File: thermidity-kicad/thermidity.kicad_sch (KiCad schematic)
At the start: 13 parts, among them J1 ISP, J2 Display, U1 ATmega328P-P, U2 MCP1501-30xSN, U3 TMP36GT9, U4 HIH-5030-001

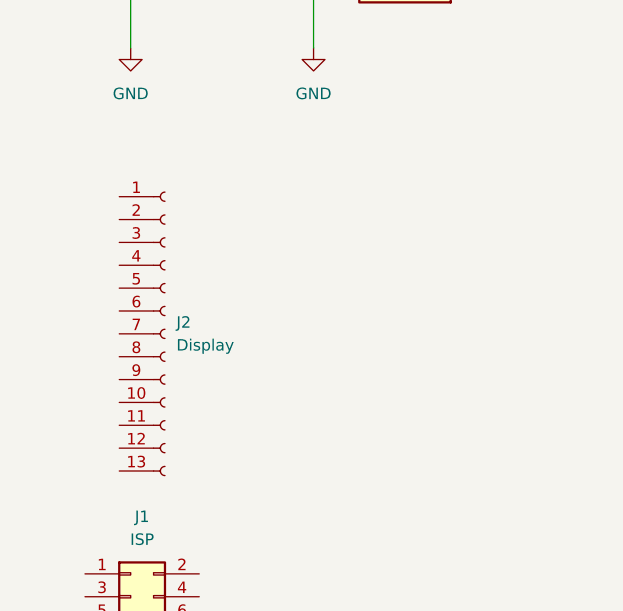
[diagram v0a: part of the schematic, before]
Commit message: update README, add crystal to schematic
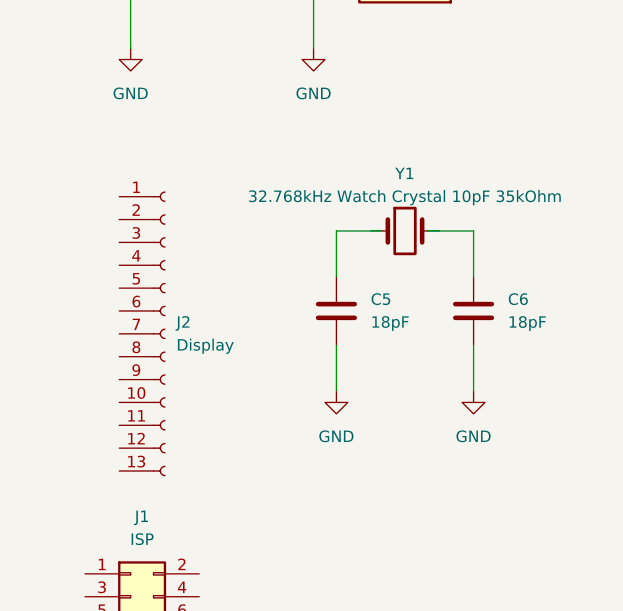
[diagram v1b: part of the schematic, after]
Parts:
- added C5, C6: 18pF, Capacitor_SMD:C_1206_3216Metric_Pad1.33x1.80mm_HandSolder, symbol Device:C
- added Y1: 32.768kHz Watch Crystal 10pF 35kOhm, symbol Device:Crystal
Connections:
- net GND: now also C5.2, C6.2
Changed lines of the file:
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@@
+    (stroke (width 0) (type default) (color 0 0 0 0))
+  )
+  (wire (pts (xy 214.63 113.03) (xy 214.63 118.11))
     (stroke (width 0) (type default) (color 0 0 0 0))
   )
@@
     (stroke (width 0) (type default) (color 0 0 0 0))
   )
+  (wire (pts (xy 214.63 100.33) (xy 214.63 105.41))
+    (stroke (width 0) (type default) (color 0 0 0 0))
+  )
+  (wire (pts (xy 209.55 100.33) (xy 214.63 100.33))
+    (stroke (width 0) (type default) (color 0 0 0 0))
+  )
   (wire (pts (xy 97.79 86.36) (xy 97.79 99.06))
     (stroke (width 0) (type default) (color 0 0 0 0))
@@
     (stroke (width 0) (type default) (color 0 0 0 0))
   )
+  (wire (pts (xy 199.39 100.33) (xy 199.39 105.41))
+    (stroke (width 0) (type default) (color 0 0 0 0))
+  )
   (wire (pts (xy 113.03 81.28) (xy 113.03 86.36))
     (stroke (width 0) (type default) (color 0 0 0 0))
@@
     (stroke (width 0) (type default) (color 0 0 0 0))
   )
+  (wire (pts (xy 199.39 113.03) (xy 199.39 118.11))
+    (stroke (width 0) (type default) (color 0 0 0 0))
+  )
   (wire (pts (xy 128.27 121.92) (xy 128.27 81.28))
     (stroke (width 0) (type default) (color 0 0 0 0))
@@
   )
   (wire (pts (xy 146.05 41.91) (xy 97.79 41.91))
+    (stroke (width 0) (type default) (color 0 0 0 0))
+  )
+  (wire (pts (xy 204.47 100.33) (xy 199.39 100.33))
     (stroke (width 0) (type default) (color 0 0 0 0))
   )
@@
     (pin "1")
   )
+  (symbol (lib_id "Device:C") (at 199.39 109.22 0) (unit 1)
+    (in_bom yes) (on_board yes) (fields_autoplaced)
+    (property "Reference" "C5" (id 0) (at 203.2 107.9499 0)
+      (effects (font (size 1.27 1.27)) (justify left))
+    )
+    (property "Value" "18pF" (id 1) (at 203.2 110.4899 0)
+      (effects (font (size 1.27 1.27)) (justify left))
+    )
+    (property "Footprint" "Capacitor_SMD:C_1206_3216Metric_Pad1.33x1.80mm_HandSolder" (id 2) (at 200.3552 113.03 0)
+      (effects (font (size 1.27 1.27)) hide)
+    )
+    (property "Datasheet" "~" (id 3) (at 199.39 109.22 0)
+      (effects (font (size 1.27 1.27)) hide)
+    )
+    (pin "1")
+    (pin "2")
+  )
   (symbol (lib_id "power:GND") (at 128.27 57.15 0) (unit 1)
     (in_bom yes) (on_board yes) (fields_autoplaced)
@@
     (pin "6")
   )
+  (symbol (lib_id "Device:Crystal") (at 207.01 100.33 0) (unit 1)
+    (in_bom yes) (on_board yes) (fields_autoplaced)
+    (property "Reference" "Y1" (id 0) (at 207.01 93.98 0))
+    (property "Value" "32.768kHz Watch Crystal 10pF 35kOhm" (id 1) (at 207.01 96.52 0))
+    (property "Footprint" "" (id 2) (at 207.01 100.33 0)
+      (effects (font (size 1.27 1.27)) hide)
+    )
+    (property "Datasheet" "~" (id 3) (at 207.01 100.33 0)
+      (effects (font (size 1.27 1.27)) hide)
+    )
+    (pin "1")
+    (pin "2")
+  )
   (symbol (lib_id "power:+BATT") (at 146.05 41.91 0) (unit 1)
     (in_bom yes) (on_board yes) (fields_autoplaced)
@@
     )
     (property "Datasheet" "" (id 3) (at 82.55 64.77 0)
+      (effects (font (size 1.27 1.27)) hide)
+    )
+    (pin "1")
+  )
+  (symbol (lib_id "power:GND") (at 199.39 118.11 0) (unit 1)
+    (in_bom yes) (on_board yes) (fields_autoplaced)
+    (property "Reference" "#PWR?" (id 0) (at 199.39 124.46 0)
+      (effects (font (size 1.27 1.27)) hide)
+    )
+    (property "Value" "GND" (id 1) (at 199.39 123.19 0))
+    (property "Footprint" "" (id 2) (at 199.39 118.11 0)
+      (effects (font (size 1.27 1.27)) hide)
+    )
+    (property "Datasheet" "" (id 3) (at 199.39 118.11 0)
       (effects (font (size 1.27 1.27)) hide)
     )
@@
     (pin "9")
   )
+  (symbol (lib_id "power:GND") (at 214.63 118.11 0) (unit 1)
+    (in_bom yes) (on_board yes) (fields_autoplaced)
+    (property "Reference" "#PWR?" (id 0) (at 214.63 124.46 0)
+      (effects (font (size 1.27 1.27)) hide)
+    )
+    (property "Value" "GND" (id 1) (at 214.63 123.19 0))
+    (property "Footprint" "" (id 2) (at 214.63 118.11 0)
+      (effects (font (size 1.27 1.27)) hide)
+    )
+    (property "Datasheet" "" (id 3) (at 214.63 118.11 0)
+      (effects (font (size 1.27 1.27)) hide)
+    )
+    (pin "1")
+  )
   (symbol (lib_id "Reference_Voltage:MCP1501-30xSN") (at 97.79 78.74 0) (unit 1)
     (in_bom yes) (on_board yes) (fields_autoplaced)
@@
     (pin "1")
   )
+  (symbol (lib_id "Device:C") (at 214.63 109.22 0) (unit 1)
+    (in_bom yes) (on_board yes) (fields_autoplaced)
+    (property "Reference" "C6" (id 0) (at 218.44 107.9499 0)
+      (effects (font (size 1.27 1.27)) (justify left))
+    )
+    (property "Value" "18pF" (id 1) (at 218.44 110.4899 0)
+      (effects (font (size 1.27 1.27)) (justify left))
+    )
+    (property "Footprint" "Capacitor_SMD:C_1206_3216Metric_Pad1.33x1.80mm_HandSolder" (id 2) (at 215.5952 113.03 0)
+      (effects (font (size 1.27 1.27)) hide)
+    )
+    (property "Datasheet" "~" (id 3) (at 214.63 109.22 0)
+      (effects (font (size 1.27 1.27)) hide)
+    )
+    (pin "1")
+    (pin "2")
+  )
   (symbol (lib_id "Device:R") (at 120.65 135.89 0) (unit 1)
     (in_bom yes) (on_board yes) (fields_autoplaced)
@@
       (reference "#PWR?") (unit 1) (value "GND") (footprint "")
     )
+    (path "/94bf8396-b53e-48d7-867c-3779df6a12e4"
+      (reference "#PWR?") (unit 1) (value "GND") (footprint "")
+    )
     (path "/a2d0e6a7-6199-4702-be53-1953075dda18"
+      (reference "#PWR?") (unit 1) (value "GND") (footprint "")
+    )
+    (path "/bf845653-5bee-4a32-b784-08641f731c62"
       (reference "#PWR?") (unit 1) (value "GND") (footprint "")
     )
@@
       (reference "C4") (unit 1) (value "100nF") (footprint "Capacitor_SMD:C_1206_3216Metric_Pad1.33x1.80mm_HandSolder")
     )
+    (path "/2782ed05-b38e-4160-a854-e129bce2a00e"
+      (reference "C5") (unit 1) (value "18pF") (footprint "Capacitor_SMD:C_1206_3216Metric_Pad1.33x1.80mm_HandSolder")
+    )
+    (path "/cd47be7e-fc20-4cc3-8eef-45df9b7c371f"
+      (reference "C6") (unit 1) (value "18pF") (footprint "Capacitor_SMD:C_1206_3216Metric_Pad1.33x1.80mm_HandSolder")
+    )
     (path "/60063fea-c781-49af-81c6-4ddf33326155"
       (reference "J1") (unit 1) (value "ISP") (footprint "")
@@
       (reference "U4") (unit 1) (value "HIH-5030-001") (footprint "HONEYWELL_HIH-5030-001")
     )
-  )
+    (path "/6d70419f-6fb5-4d41-b7b0-0e8b0be22d14"
+      (reference "Y1") (unit 1) (value "32.768kHz Watch Crystal 10pF 35kOhm") (footprint "")
+    )
+  )
